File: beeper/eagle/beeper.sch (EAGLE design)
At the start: 32 parts, among them Q1 16MHz, T1 3904, U1 ATMEGA328P, U2 ATA6631

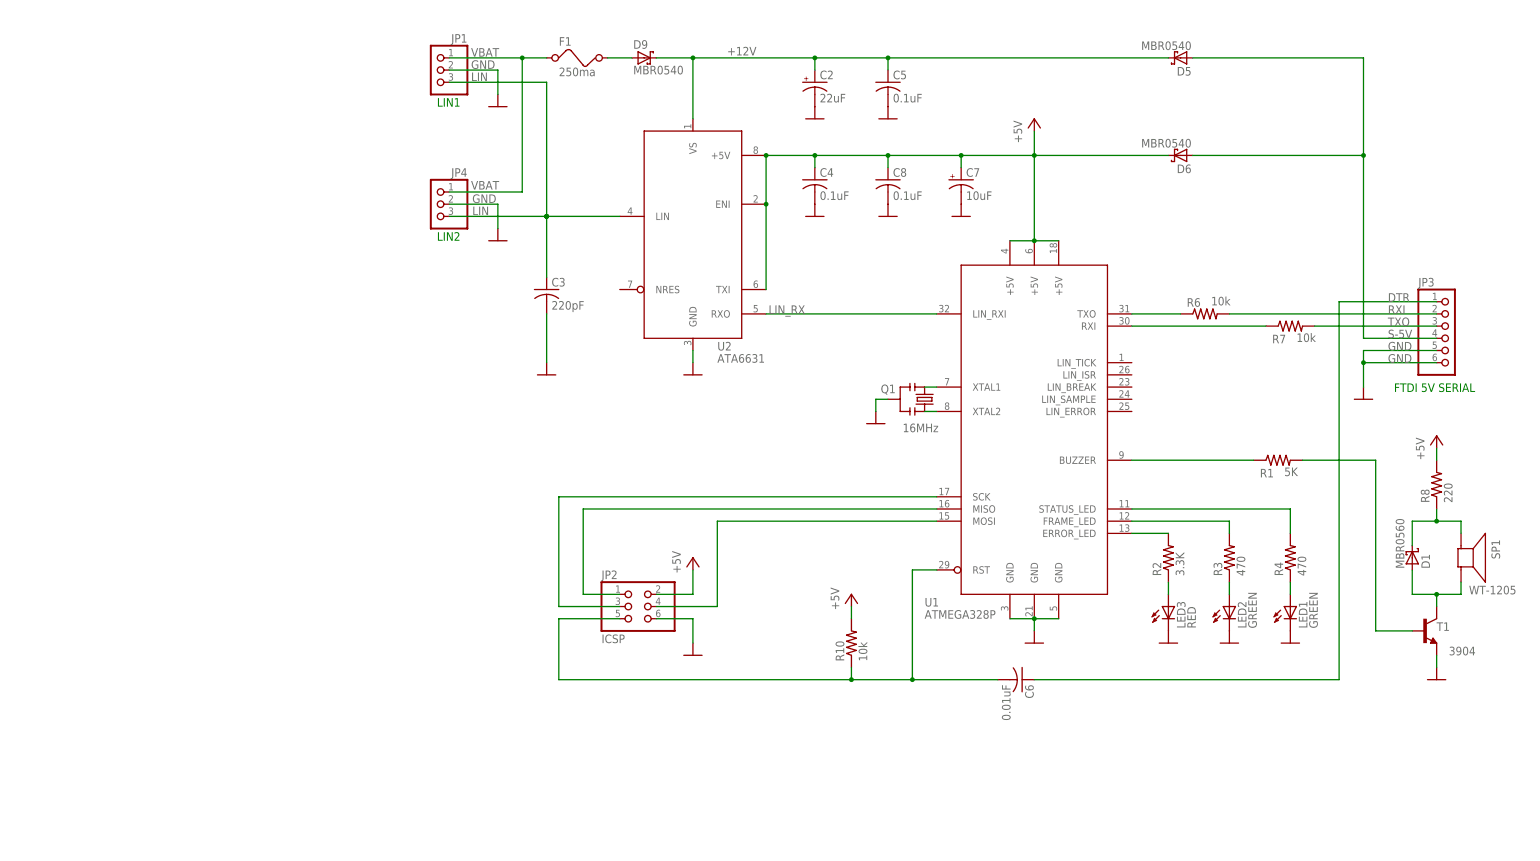
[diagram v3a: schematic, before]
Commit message: First complete routing. Still needs TLC.
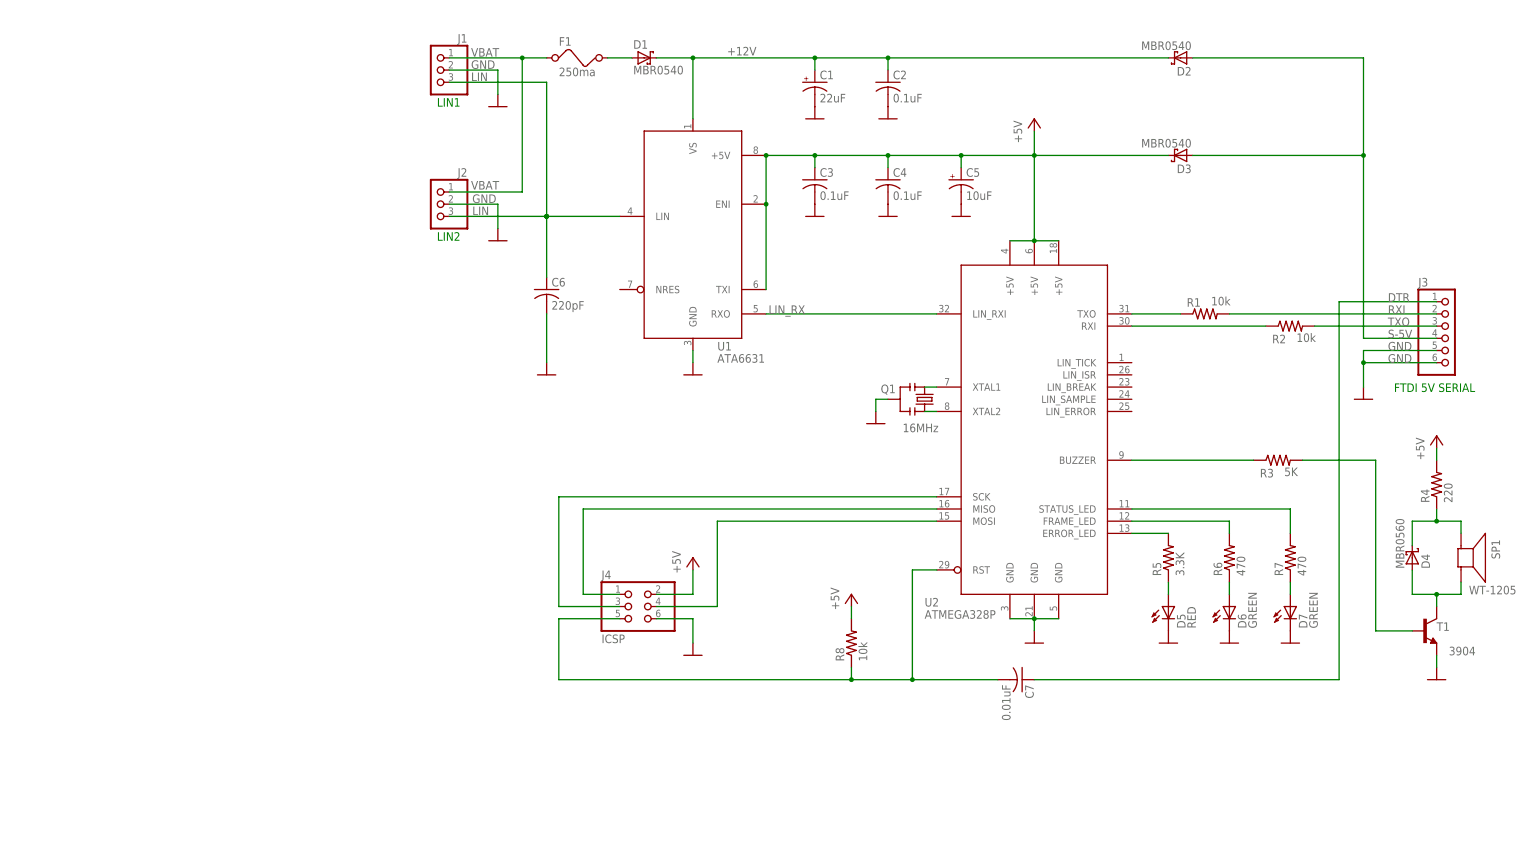
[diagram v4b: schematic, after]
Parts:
- removed C8: 0.1uF, rcl:C-USC0805
- removed D9: MBR0540, diode:SMF5.0AT1
- removed LED2: GREEN, led:LEDSMT1206
- removed LED3: RED, led:LEDSMT1206
- removed R10: 10k, rcl:R-US_R0805
- added C1: 22uF, rcl:CPOL-USUD-6,3X5,8
- added D2, D3: MBR0540, diode:SMF5.0AT1
- added D4: MBR0560, diode:SMF5.0AT1
- added R5: 3.3K, rcl:R-US_R0805
- C2: value 22uF -> 0.1uF; device rcl:CPOL-USUD-6,3X5,8 -> rcl:C-USC0805
- C3: value 220pF -> 0.1uF
- C5: value 0.1uF -> 10uF; device rcl:C-USC0805 -> rcl:CPOL-USA/3216-18R
- C6: value 0.01uF -> 220pF
- C7: value 10uF -> 0.01uF; device rcl:CPOL-USA/3216-18R -> rcl:C-USC0805
- D1: value MBR0560 -> MBR0540
- D5: value MBR0540 -> RED; device diode:SMF5.0AT1 -> led:LEDSMT1206
- D6: value MBR0540 -> GREEN; device diode:SMF5.0AT1 -> led:LEDSMT1206
- R1: value 5K -> 10k
- R2: value 3.3K -> 10k
- R3: value 470 -> 5K
- R4: value 470 -> 220
- R6, R7: value 10k -> 470
- R8: value 220 -> 10k
- U1: value ATMEGA328P -> ATA6631; device beeper:ATMEGA328P -> beeper:ATA6631
- U2: value ATA6631 -> ATMEGA328P; device beeper:ATA6631 -> beeper:ATMEGA328P
- renumbered JP1 to J1, JP2 to J4, JP3 to J3, JP4 to J2, LED1 to D7
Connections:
- removed net N$1: Q1.3, U1.XTAL1
- removed net N$11: Q1.1, U1.XTAL2
- new net XTAL1: Q1.3, U2.XTAL1
- new net XTAL2: Q1.1, U2.XTAL2
- net +12V: now also C1.+, C2.1, D1.C, D2.C, U1.VS; no longer C2.+, C5.1, D5.C, D9.C, U2.VS
- net +5V: now also C3.1, C5.+, D3.C, R4.2, U1.+5V, U1.ENI, U1.TXI, U2.+5V@1, U2.+5V@2, U2.+5V@3; no longer C7.+, C8.1, D6.C, R10.2, U1.+5V@1, U1.+5V@2, U1.+5V@3, U2.+5V, U2.ENI, U2.TXI
- net DTR: now also C7.1; no longer C6.1
- net GND: now also C1.-, C2.2, C5.-, C6.2, D5.C, D6.C, U1.GND, U2.GND@1, U2.GND@2, U2.GND@3; no longer C2.-, C5.2, C7.-, C8.2, LED2.C, LED3.C, U1.GND@1, U1.GND@2, U1.GND@3, U2.GND
- net LIN: now also C6.1, U1.LIN; no longer C3.1, U2.LIN
- net LIN_RX: now also U1.RXO, U2.LIN_RXI; no longer U1.LIN_RXI, U2.RXO
- net N$14: now also R2.1, U2.RXI; no longer R7.1, U1.RXI
- net N$15: now also C7.2, R8.1, U2.RST; no longer C6.2, R10.1, U1.RST
- net N$17: now also R3.1, U2.BUZZER; no longer R1.1, U1.BUZZER
- net N$19: now also R3.2; no longer R1.2
- net N$2: now also R7.1; no longer R4.1
- net N$20: now also U2.MOSI; no longer U1.MOSI
- net N$22: now also R1.1, U2.TXO; no longer R6.1, U1.TXO
- net N$25: now also U2.MISO; no longer U1.MISO
- net N$28: now also U2.SCK; no longer U1.SCK
- net N$3: now also D6.A, R6.1; no longer LED2.A, R3.1
- net N$30: now also D4.C, R4.1; no longer D1.C, R8.1
- net N$31: now also D4.A; no longer D1.A
- net N$4: now also D5.A, R5.1; no longer LED3.A, R2.1
- net N$6: now also D1.A; no longer D9.A
- net N$7: now also R5.2, U2.ERROR_LED; no longer R2.2, U1.ERROR_LED
- net N$8: now also R6.2, U2.FRAME_LED; no longer R3.2, U1.FRAME_LED
- net N$9: now also R7.2, U2.STATUS_LED; no longer R4.2, U1.STATUS_LED
- net RXI: now also R1.2; no longer R6.2
- net S-5V: now also D2.A, D3.A; no longer D5.A, D6.A
- net TXO: now also R2.2; no longer R7.2
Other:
- moved on the sheet: C3, C4, C6, D1, R1, R2, R3, R4, R6, R7, R8

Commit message: Made the pads of the resonator longer for easy soldering. Tweaked the layout.
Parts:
- Q1: device SparkFun:RESONATORSMD -> beeper:RESONATORSMD
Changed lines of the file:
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@@
 <part name="D2" library="diode" deviceset="SMF5.0AT1" device="" value="MBR0540"/>
 <part name="D3" library="diode" deviceset="SMF5.0AT1" device="" value="MBR0540"/>
-<part name="Q1" library="SparkFun" deviceset="RESONATOR" device="SMD" value="16MHz"/>
+<part name="Q1" library="beeper" deviceset="RESONATOR" device="SMD" value="16MHz"/>
 <part name="GND8" library="beeper" deviceset="GND" device=""/>
 <part name="SP1" library="beeper" deviceset="AL60P" device="" value="WT-1205"/>

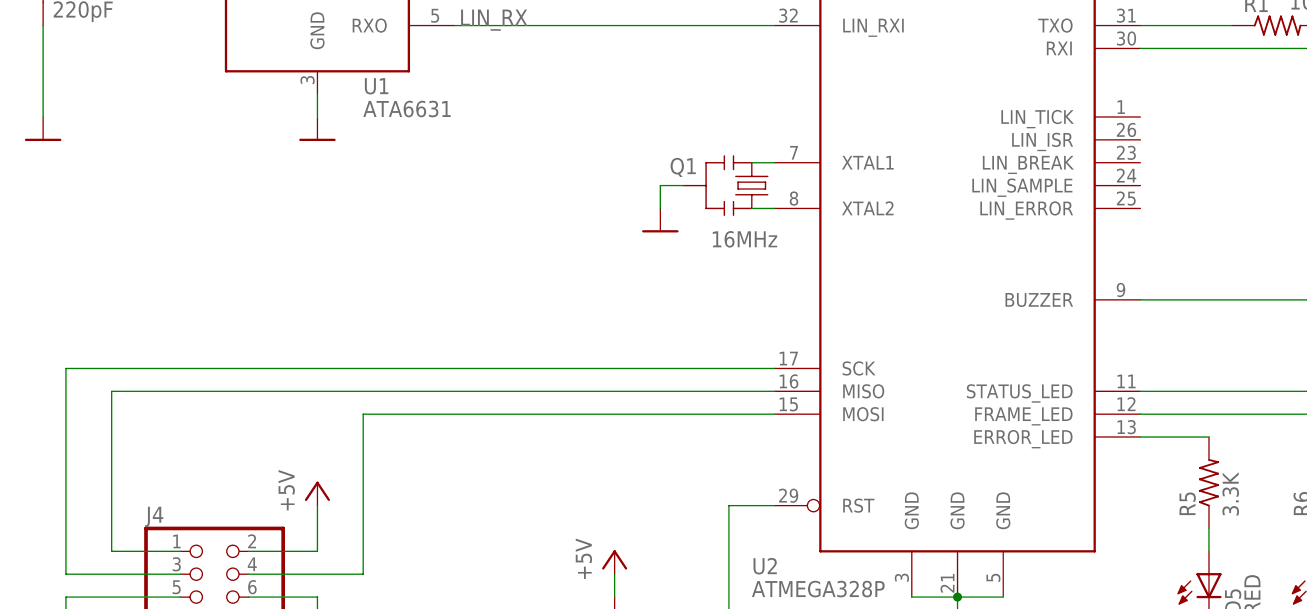
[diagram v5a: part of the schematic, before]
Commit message: Moved two debug pins to MISO/MOSI to free I/O pins.
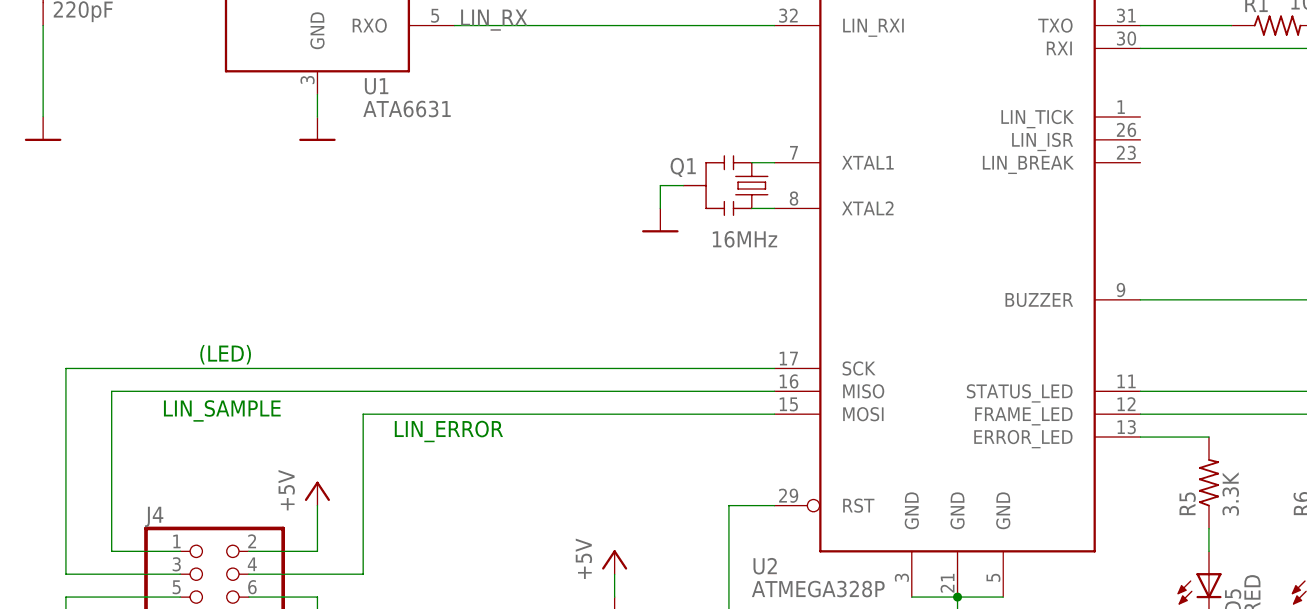
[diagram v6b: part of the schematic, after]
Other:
- note added: "(LED)"
- note added: "LIN_ERROR"
- note added: "LIN_SAMPLE"
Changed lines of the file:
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@@
 <text x="76.2" y="162.56" size="1.778" layer="91">LIN2</text>
 <text x="275.59" y="131.064" size="1.778" layer="91">FTDI 5V SERIAL</text>
+<text x="137.922" y="101.6" size="1.778" layer="91">LIN_ERROR</text>
+<text x="112.268" y="103.886" size="1.778" layer="91">LIN_SAMPLE</text>
+<text x="116.332" y="109.982" size="1.778" layer="91">(LED)</text>
 </plain>
 <instances>

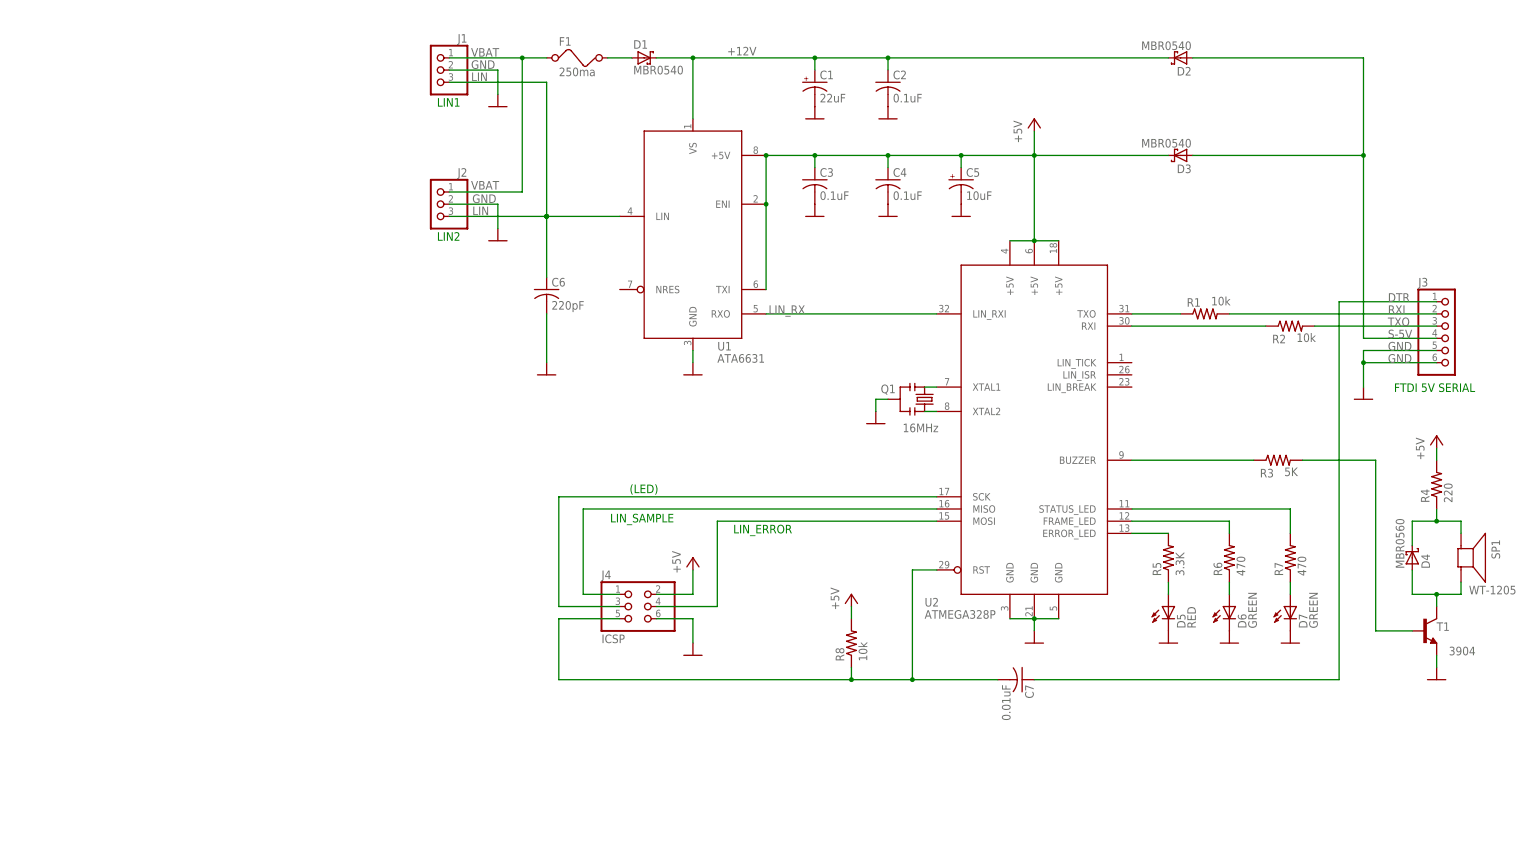
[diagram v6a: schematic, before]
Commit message: Updated annotations of beeper schematic. No semantic changes.
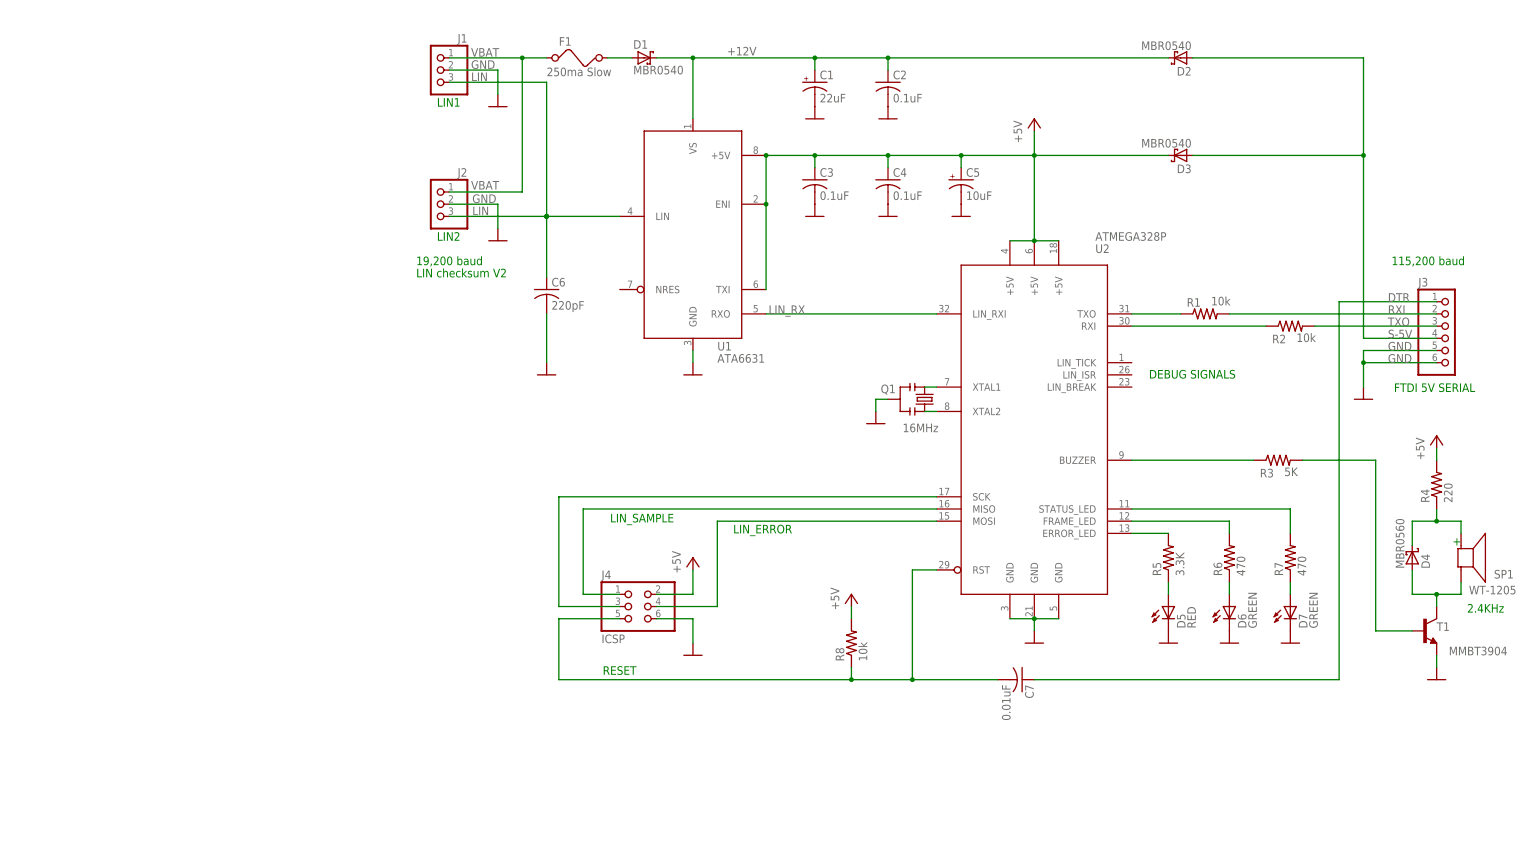
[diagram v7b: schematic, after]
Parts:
- F1: value 250ma -> 250ma Slow
- T1: value 3904 -> MMBT3904
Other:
- note added: "+"
- note added: "115,200 baud"
- note added: "19,200 baud"
- note added: "2.4KHz"
- note added: "DEBUG SIGNALS"
- note added: "LIN checksum V2"
- note added: "RESET"
- note removed: "(LED)"
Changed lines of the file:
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@@
 <part name="P+5" library="supply1" deviceset="+5V" device=""/>
 <part name="R3" library="rcl" deviceset="R-US_" device="R0805" value="5K"/>
-<part name="T1" library="transistor" deviceset="*-NPN-" device="SOT23-BEC" technology="MMBT3904LT1" value="3904"/>
+<part name="T1" library="transistor" deviceset="*-NPN-" device="SOT23-BEC" technology="MMBT3904LT1" value="MMBT3904"/>
 <part name="GND18" library="beeper" deviceset="GND" device=""/>
 <part name="P+3" library="supply1" deviceset="+5V" device=""/>
@@
 <part name="GND17" library="beeper" deviceset="GND" device=""/>
 <part name="GND11" library="beeper" deviceset="GND" device=""/>
-<part name="F1" library="beeper" deviceset="FUSE" device="" value="250ma"/>
+<part name="F1" library="beeper" deviceset="FUSE" device="" value="250ma Slow"/>
 </parts>
 <sheets>
@@
 <text x="137.922" y="101.6" size="1.778" layer="91">LIN_ERROR</text>
 <text x="112.268" y="103.886" size="1.778" layer="91">LIN_SAMPLE</text>
-<text x="116.332" y="109.982" size="1.778" layer="91">(LED)</text>
+<text x="110.744" y="72.136" size="1.778" layer="91">RESET</text>
+<text x="275.082" y="157.48" size="1.778" layer="91">115,200 baud</text>
+<text x="71.882" y="157.48" size="1.778" layer="91">19,200 baud</text>
+<text x="290.83" y="85.09" size="1.778" layer="91">2.4KHz</text>
+<text x="287.782" y="99.06" size="1.778" layer="91">+</text>
+<text x="224.536" y="133.858" size="1.778" layer="91">DEBUG SIGNALS</text>
+<text x="71.882" y="154.94" size="1.778" layer="91">LIN checksum V2</text>
 </plain>
 <instances>
@@
 <instance part="D1" gate="G$1" x="119.38" y="200.66"/>
 <instance part="U2" gate="G$1" x="200.66" y="127" smashed="yes">
-<attribute name="VALUE" x="177.8" y="83.82" size="1.778" layer="96"/>
-<attribute name="NAME" x="177.8" y="86.36" size="1.778" layer="95"/>
+<attribute name="VALUE" x="213.36" y="162.56" size="1.778" layer="96"/>
+<attribute name="NAME" x="213.36" y="160.02" size="1.778" layer="95"/>
 </instance>
 <instance part="D2" gate="G$1" x="231.14" y="200.66" rot="R180"/>
@@
 <instance part="GND8" gate="1" x="167.64" y="124.46"/>
 <instance part="SP1" gate="G$1" x="289.56" y="96.52" smashed="yes" rot="R270">
-<attribute name="NAME" x="295.91" y="100.33" size="1.778" layer="95" rot="R270"/>
+<attribute name="NAME" x="296.418" y="92.202" size="1.778" layer="95"/>
 <attribute name="VALUE" x="291.211" y="88.9" size="1.778" layer="96"/>
 </instance>
@@
 <instance part="GND17" gate="1" x="170.18" y="187.96"/>
 <instance part="GND11" gate="1" x="129.54" y="134.62"/>
-<instance part="F1" gate="G$1" x="106.68" y="200.66"/>
+<instance part="F1" gate="G$1" x="106.68" y="200.66" smashed="yes">
+<attribute name="NAME" x="101.6" y="203.2" size="1.778" layer="95"/>
+<attribute name="VALUE" x="99.06" y="196.85" size="1.778" layer="96"/>
+</instance>
 </instances>
 <busses>
